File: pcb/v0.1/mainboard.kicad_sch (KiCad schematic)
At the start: 0 parts

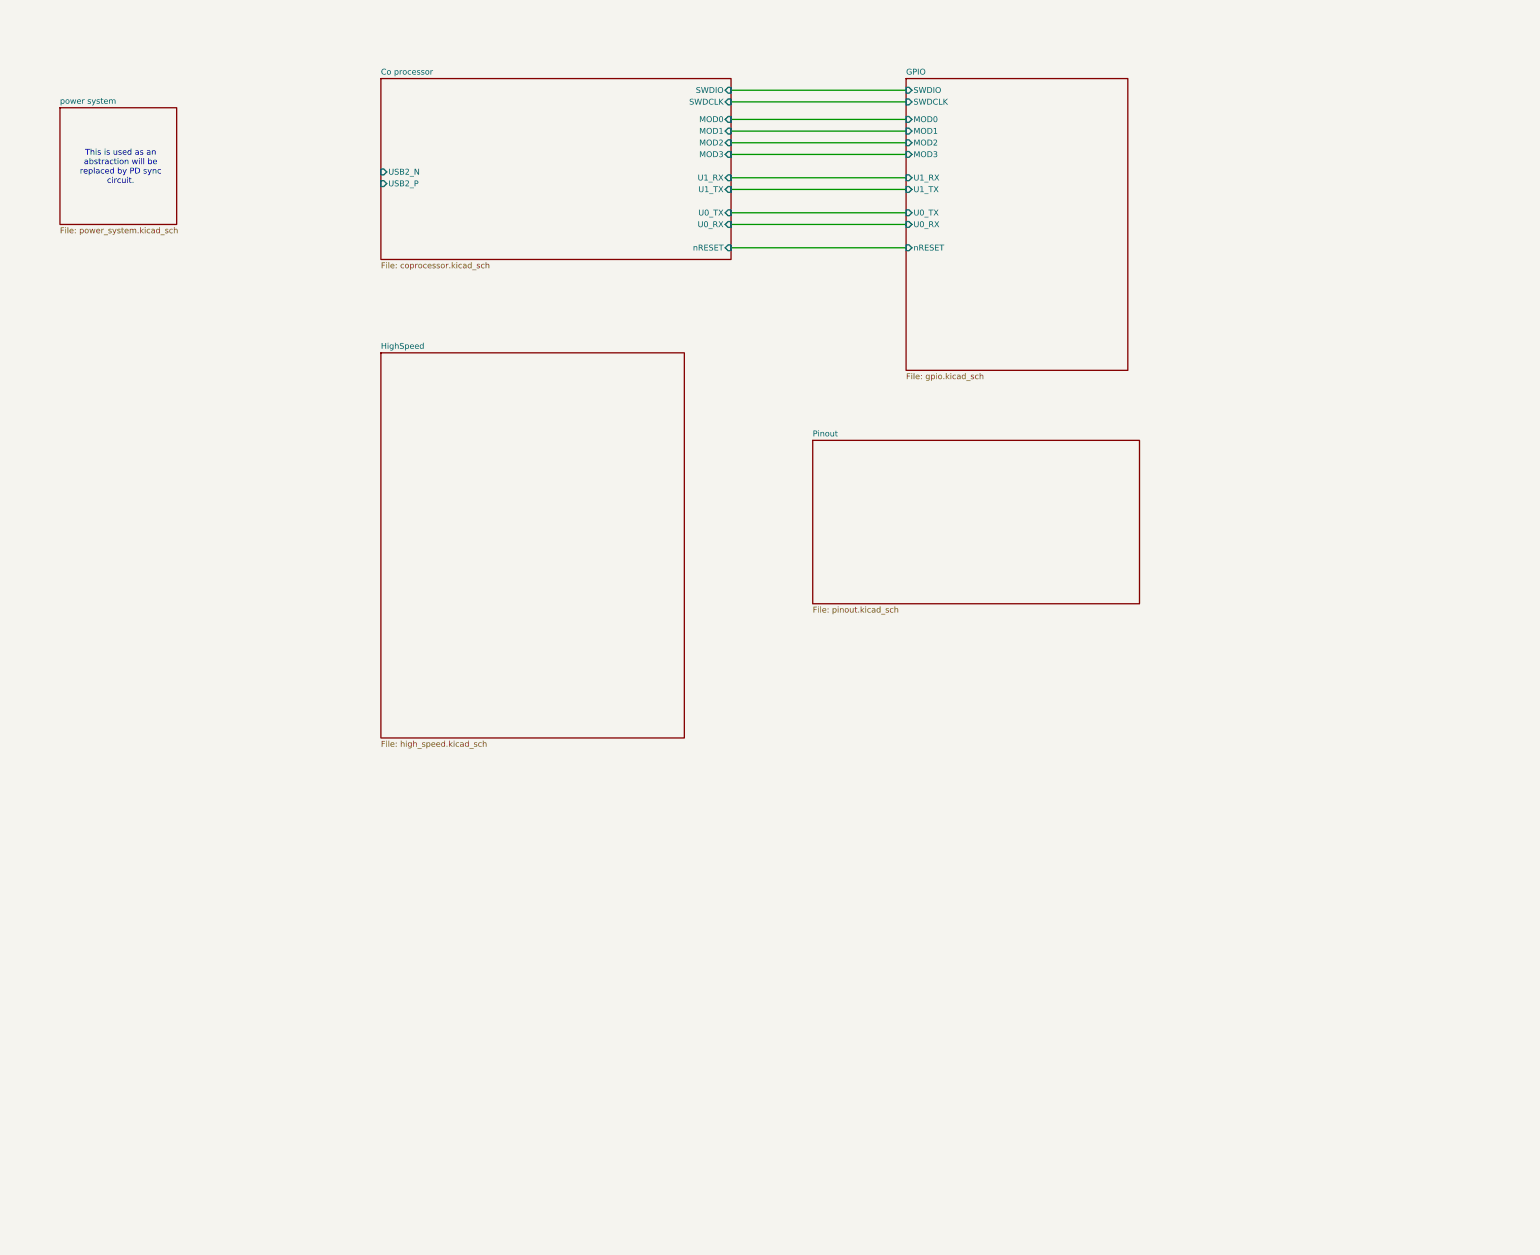
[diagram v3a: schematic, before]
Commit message: Add 3v3 regulator + reshuffle some connections.
Regulator ported over directly from PDB. I've also had to change around
some of the connections between modules to keep up with requirements.
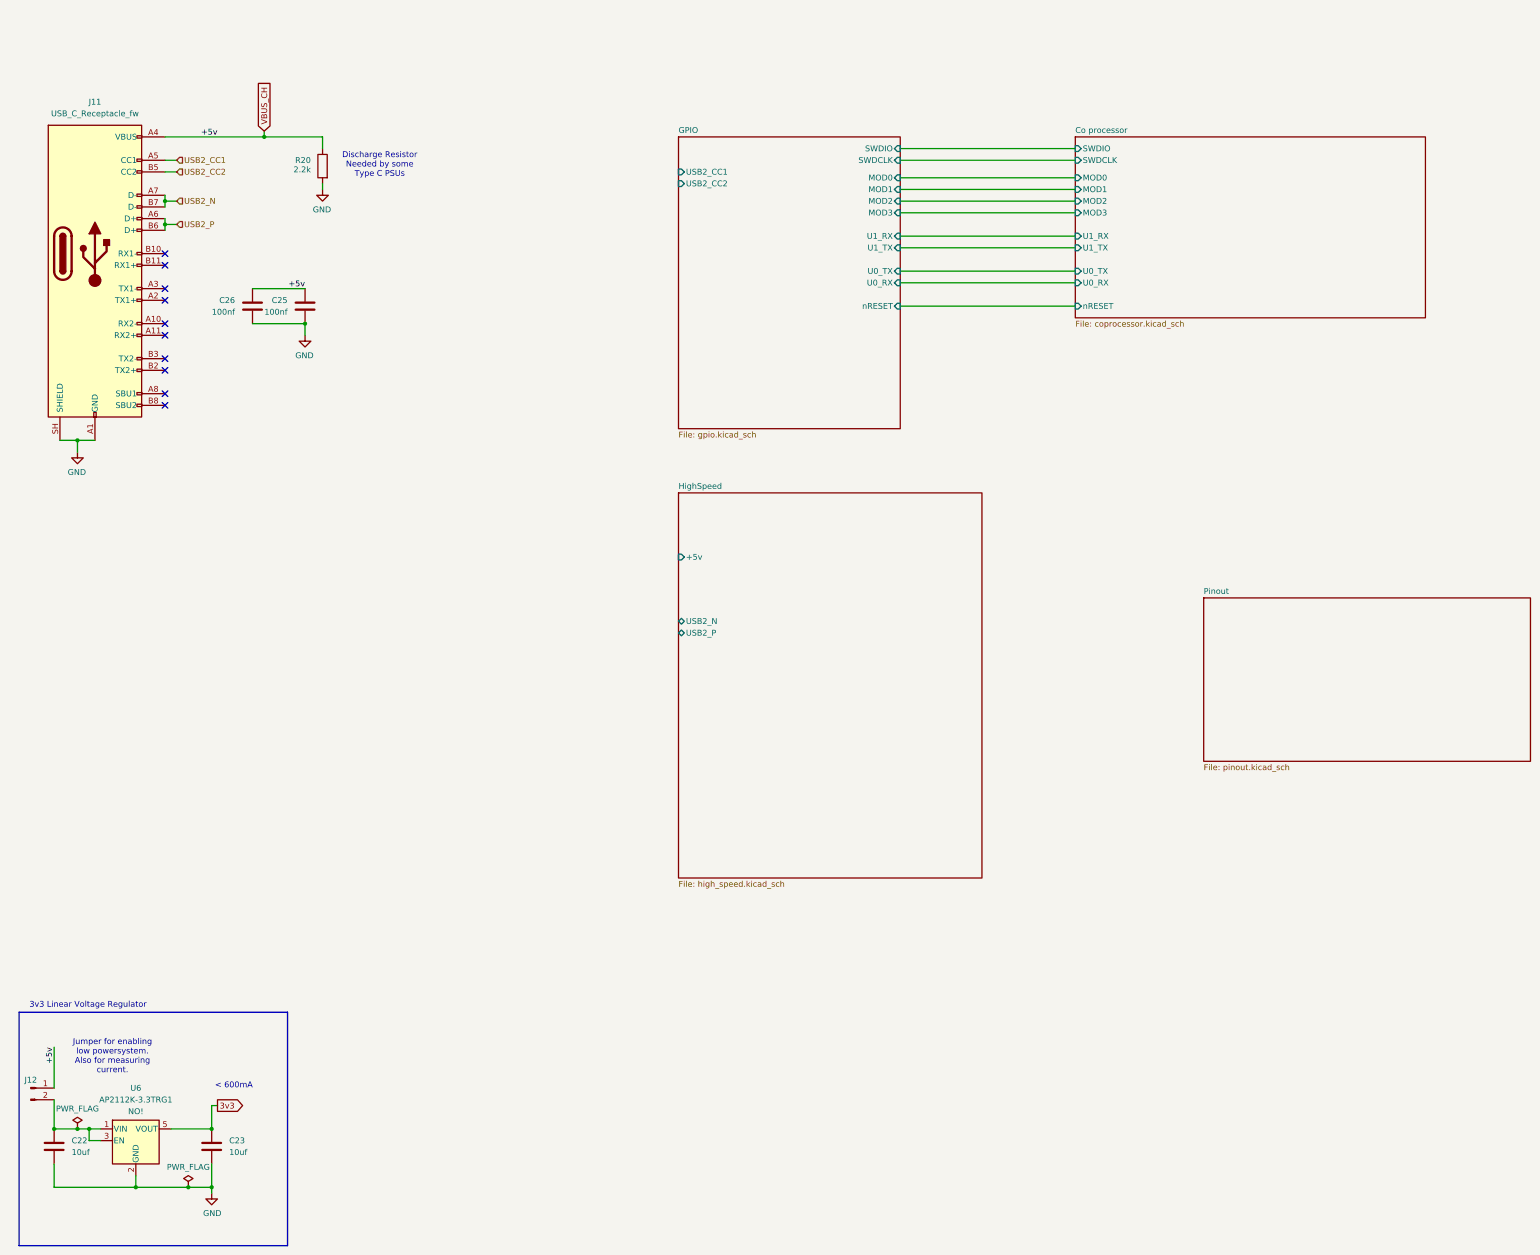
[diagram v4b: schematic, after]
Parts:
- added C22, C23: 10uf, Capacitor_SMD:C_0805_2012Metric, symbol TH-1-CC:C_10uf
- added C25, C26: 100nf, Capacitor_SMD:C_0603_1608Metric, symbol TH-1-CC:C_100nf
- added J11: USB_C_Receptacle_fw, symbol TH-1-CC:USB_C_Receptacle_fw
- added J12: Conn_01x02_Pin, symbol Connector:Conn_01x02_Pin
- added R20: 2.2k, Resistor_SMD:R_0603_1608Metric, symbol TH-1-CC:R_2.2k
- added U6: AP2112K-3.3TRG1, Package_TO_SOT_SMD:SOT-23-5, symbol TH-1-CC:AP2112K-3.3
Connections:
- new net: C22.1, J12.2 (Pin_2), U6.1 (VIN), U6.3 (EN)
- new net 3v3: C23.1, U6.5 (VOUT)
- new net GND: C22.2, C23.2, C25.2, C26.2, J11.A1 (GND), J11.A12 (GND), J11.B1 (GND), J11.B12 (GND), J11.SH (SHIELD), R20.2, U6.2 (GND)
- new net USB2_CC1: J11.A5 (CC1)
- new net USB2_CC2: J11.B5 (CC2)
- new net USB2_N: J11.A7 (D-), J11.B7 (D-)
- new net USB2_P: J11.A6 (D+), J11.B6 (D+)
- new net VBUS_CH: C25.1, C26.1, J11.A4 (VBUS), J11.A9 (VBUS), J11.B4 (VBUS), J11.B9 (VBUS), J12.1 (Pin_1), R20.1
- no-connect marks 0 -> 10
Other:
- removed sheet power system
- sheet Co processor ports: added none; removed USB2_N, USB2_P
- sheet GPIO ports: added USB2_CC1, USB2_CC2; removed none
- sheet HighSpeed ports: added +5v, USB2_N, USB2_P; removed none
- note added: "3v3 Linear Voltage Regulator"
- note added: "< 600mA"
- note added: "Discharge Resistor Needed by some Type C PSUs"
- note added: "Jumper for enabling low powersystem. Also for measuring current."
- note removed: "This is used as an abstraction will be replaced by PD sync circuit."

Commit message: Clean up main page and power rails
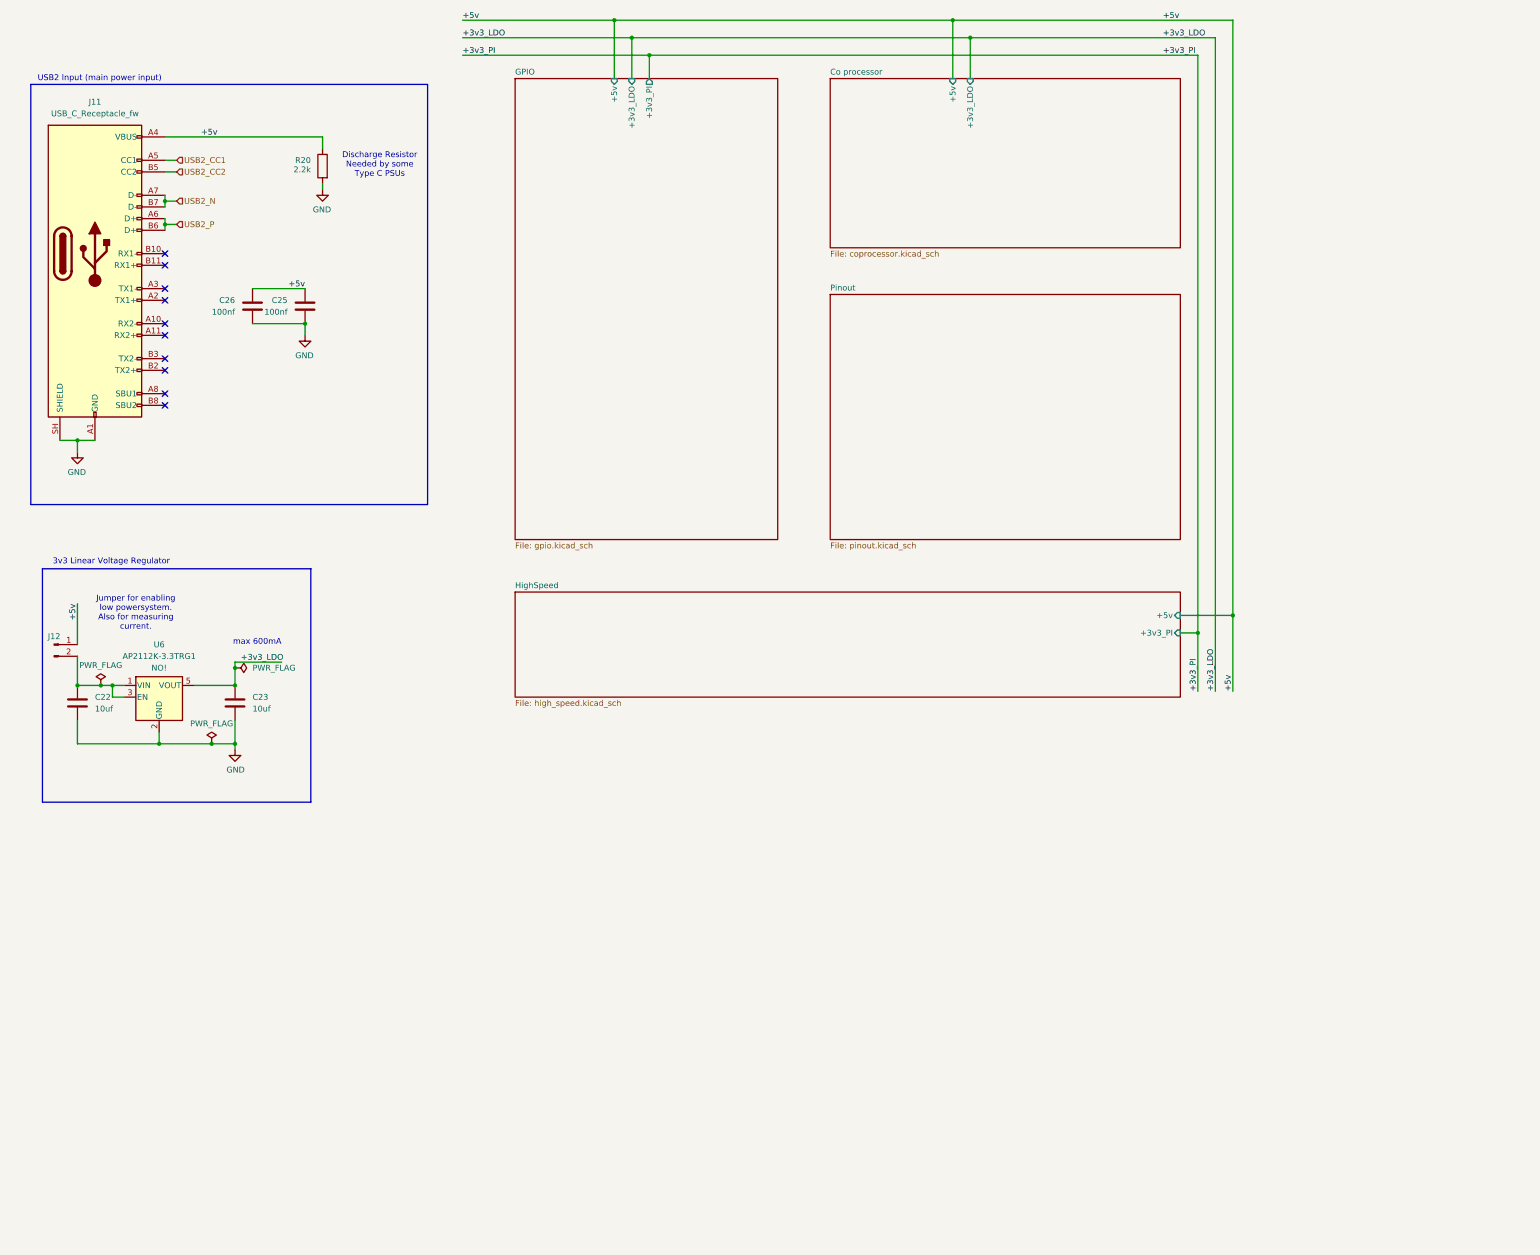
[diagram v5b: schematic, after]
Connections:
- net 3v3 renamed +3v3_LDO
- net VBUS_CH renamed +5v
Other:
- sheet Co processor ports: added +3v3_LDO, +5v; removed MOD0, MOD1, MOD2, MOD3, SWDCLK, SWDIO, U0_RX, U0_TX, U1_RX, U1_TX, nRESET
- sheet GPIO ports: added +3v3_LDO, +3v3_PI, +5v; removed MOD0, MOD1, MOD2, MOD3, SWDCLK, SWDIO, U0_RX, U0_TX, U1_RX, U1_TX, USB2_CC1, USB2_CC2, nRESET
- sheet HighSpeed ports: added +3v3_PI; removed USB2_N, USB2_P
- note added: "USB2 Input (main power input)"
- note added: "max 600mA"
- note removed: "< 600mA"
- moved on the sheet: C22, C23, J12, U6

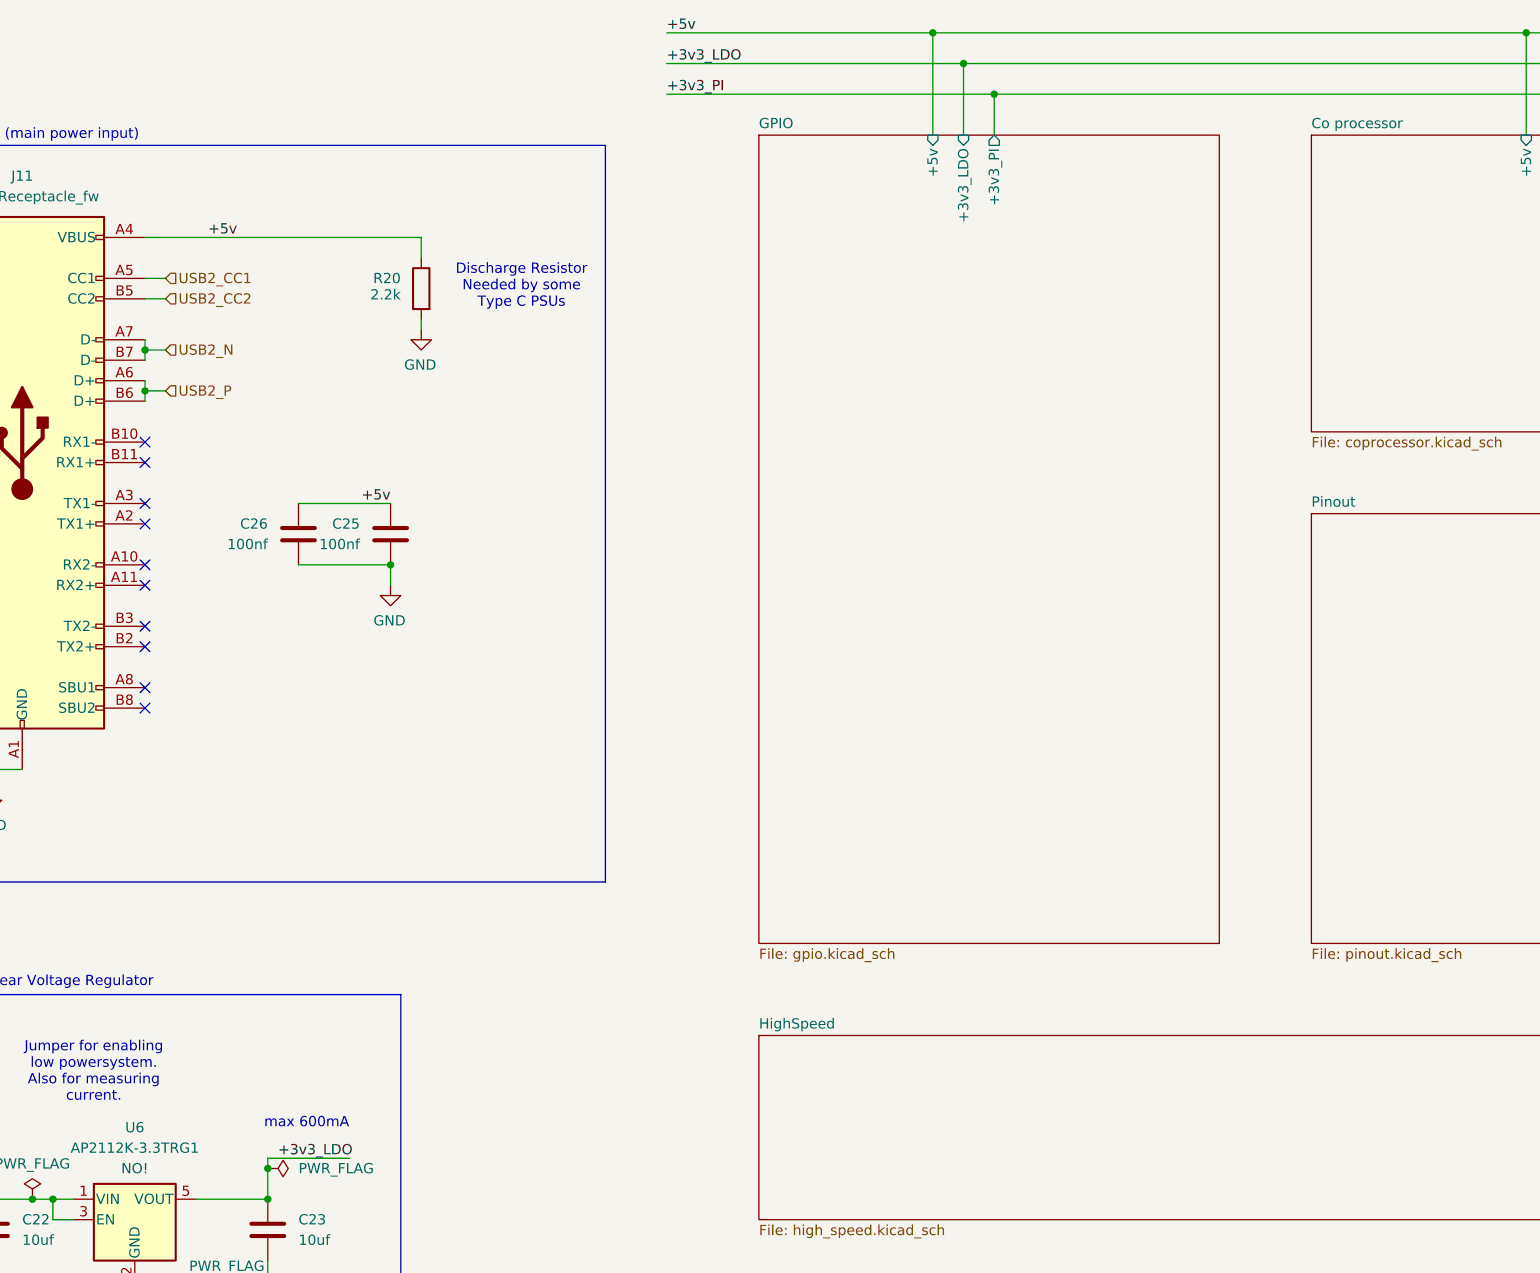
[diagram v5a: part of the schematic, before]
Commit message: Add high side switch to dac so its not draining power when pi is off
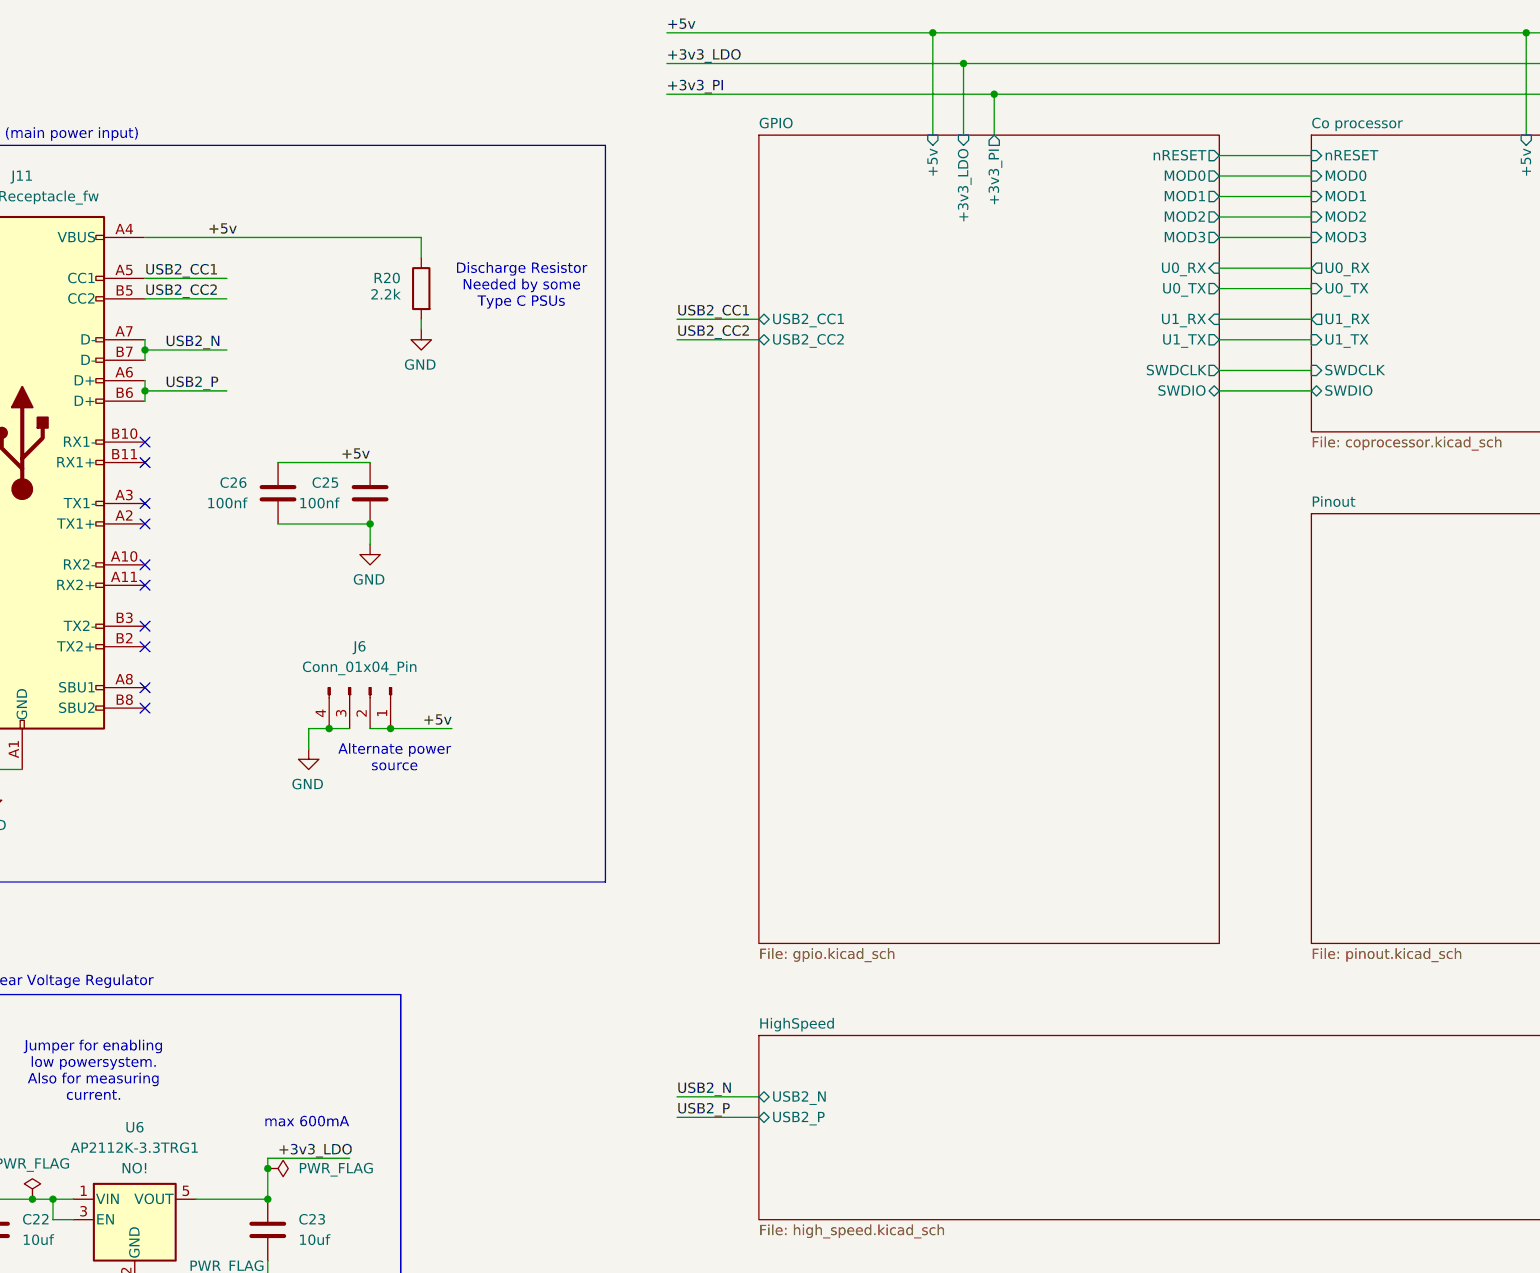
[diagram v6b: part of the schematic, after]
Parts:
- added J6: Conn_01x04_Pin, symbol Connector:Conn_01x04_Pin
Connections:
- net +5v: now also J6.1 (Pin_1), J6.2 (Pin_2)
- net GND: now also J6.3 (Pin_3), J6.4 (Pin_4)
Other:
- sheet Co processor ports: added MOD0, MOD1, MOD2, MOD3, SWDCLK, SWDIO, U0_RX, U0_TX, U1_RX, U1_TX, nRESET; removed none
- sheet GPIO ports: added MOD0, MOD1, MOD2, MOD3, SWDCLK, SWDIO, U0_RX, U0_TX, U1_RX, U1_TX, USB2_CC1, USB2_CC2, nRESET; removed none
- sheet HighSpeed ports: added USB2_N, USB2_P; removed none
- note added: "Alternate power source"
- moved on the sheet: C25, C26
